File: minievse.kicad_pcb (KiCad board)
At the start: 2 copper layers, 101.6 x 50.8 mm, 54 parts, among them IC1 ATMEGA328P-P, P1 SERIAL, P2 5V input, P3 ICSP, P4 Pilot, P5 AC_GND_AC, P6 LED_STRIP, P7 RELAY_COIL, SW1 RESET_BUTTON, U1 MAX232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

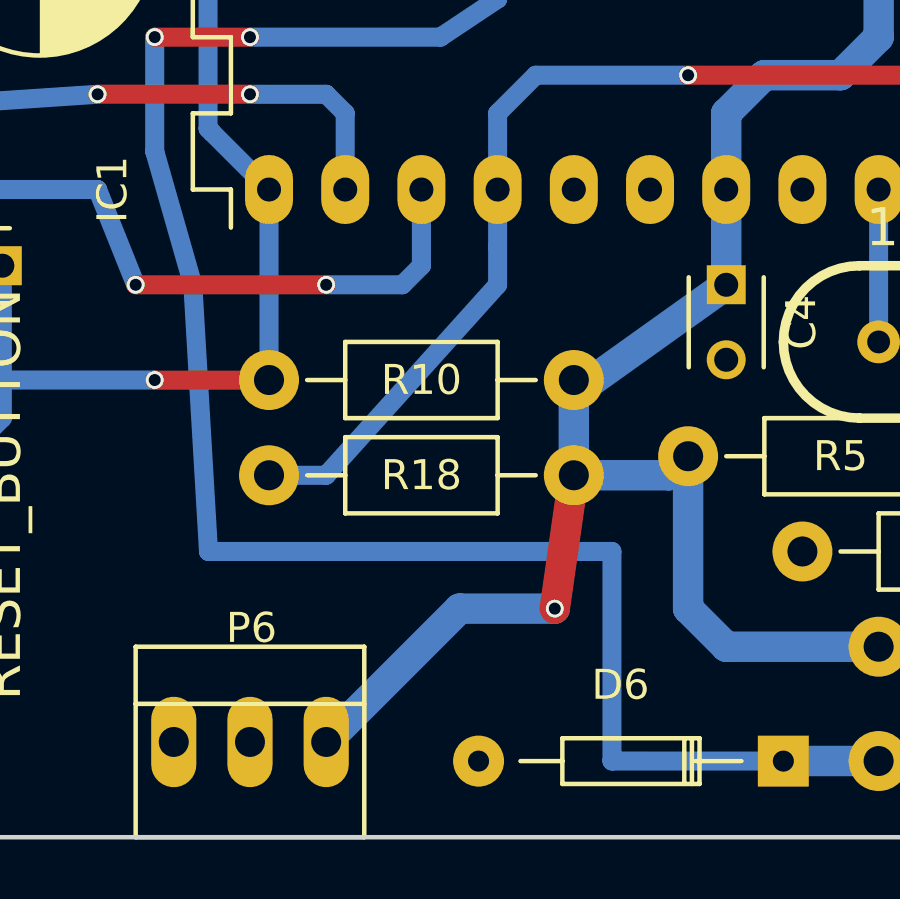
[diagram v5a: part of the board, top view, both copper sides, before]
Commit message: change LED pin from 12 to 6 for wiring convenience
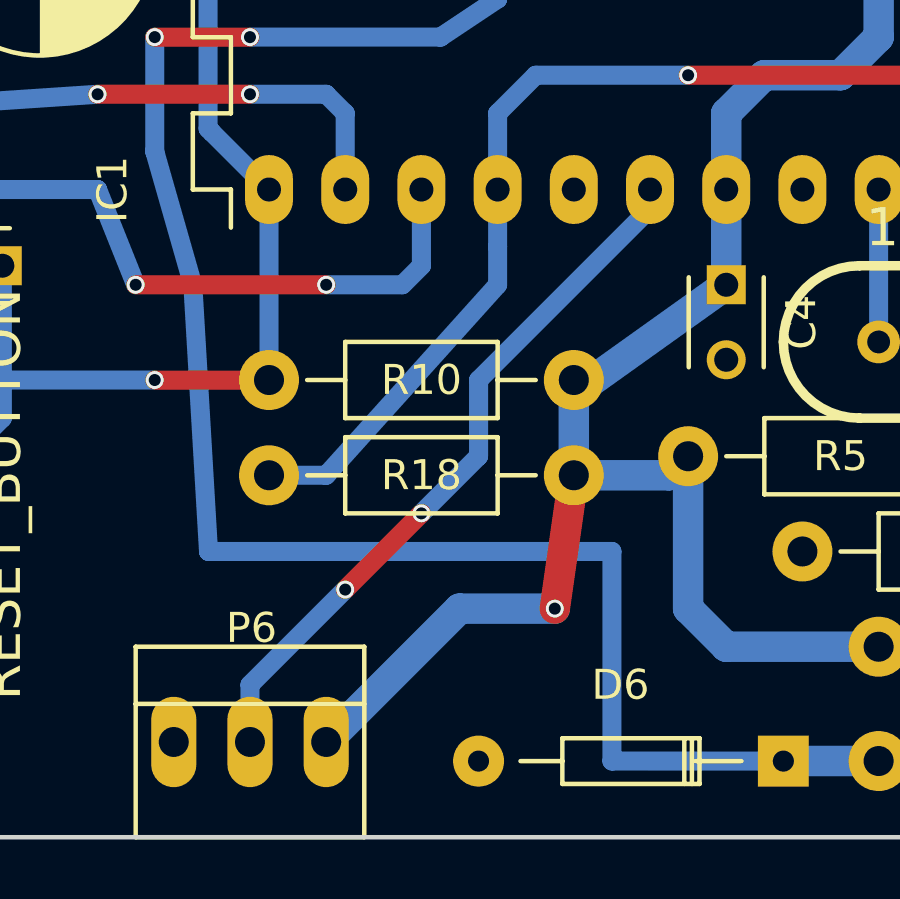
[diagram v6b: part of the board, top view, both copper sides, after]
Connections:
- IC1 pad 12: /LED_DATA -> Net-(IC1-Pad12)
- IC1 pad 6: Net-(IC1-Pad6) -> /LED_DATA
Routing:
- net /LED_DATA: track 0.00 -> 23.9 mm, vias 0 -> 2

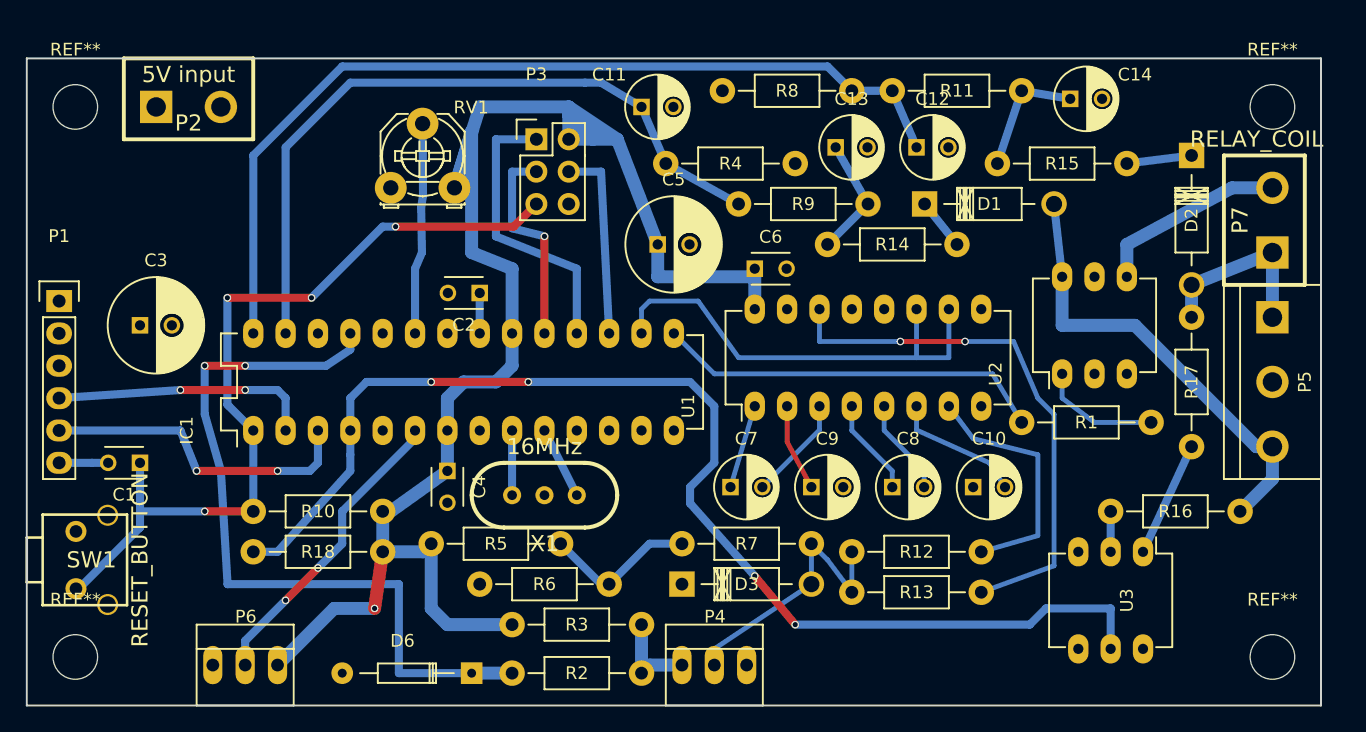
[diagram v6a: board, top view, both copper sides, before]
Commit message: finish wiring up board traces
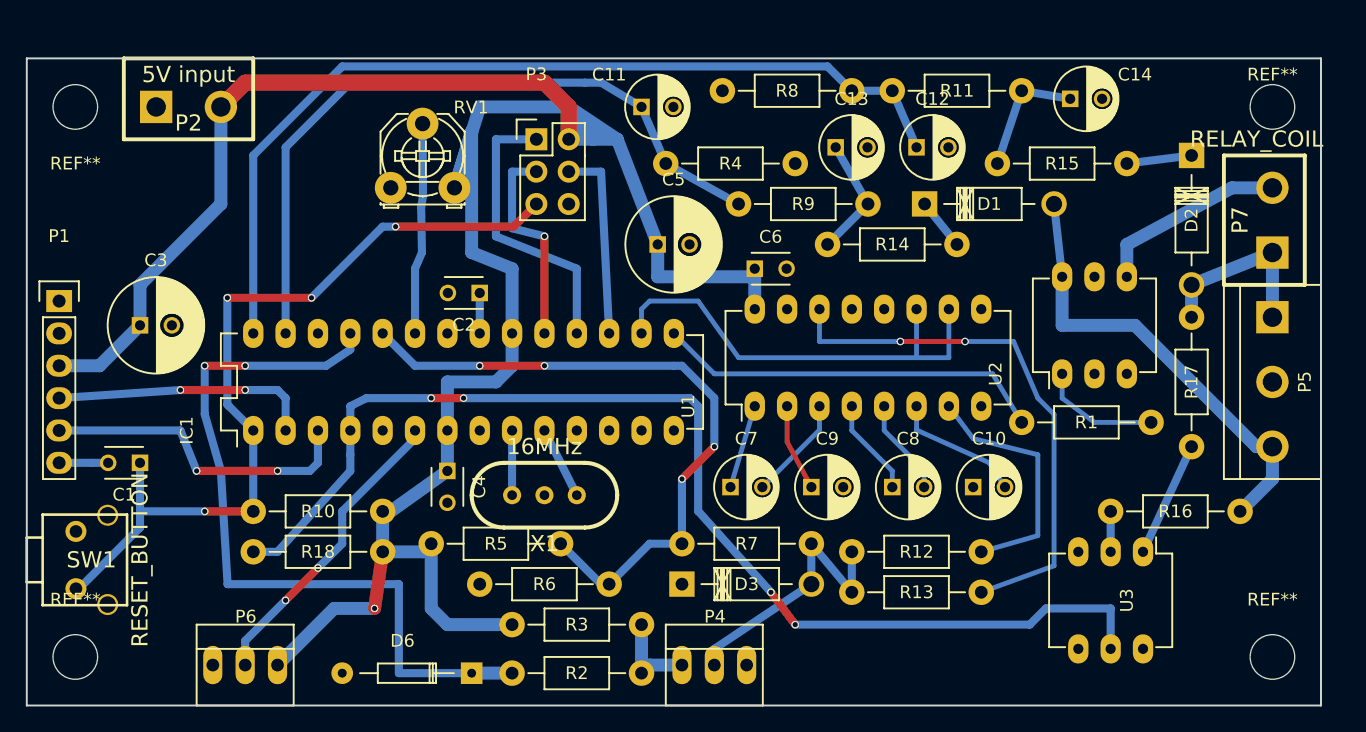
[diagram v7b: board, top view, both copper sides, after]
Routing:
- net +5VD: track 124.5 -> 184.1 mm
- net /PILOTREAD: track 12.2 -> 52.8 mm, vias 0 -> 4
- net /AC_ZEROX: track 95.5 -> 91.7 mm
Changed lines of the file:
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@@
   (general
     (links 105)
-    (no_connects 33)
-    (area 25.324999 25.324999 127.075001 76.275001)
+    (no_connects 29)
+    (area 21.006429 23.005 131.393572 78.445)
     (thickness 1.6)
     (drawings 4)
-    (tracks 244)
+    (tracks 264)
     (zones 0)
     (modules 54)
@@
     (descr "Mounting Hole 3.5mm, no annular")
     (tags "mounting hole 3.5mm no annular")
-    (fp_text reference REF** (at 0 -4.5) (layer F.SilkS)
+    (fp_text reference REF** (at 0 -2.54) (layer F.SilkS)
       (effects (font (size 1 1) (thickness 0.15)))
     )
@@
     (descr "Mounting Hole 3.5mm, no annular")
     (tags "mounting hole 3.5mm no annular")
-    (fp_text reference REF** (at 0 -4.5) (layer F.SilkS)
+    (fp_text reference REF** (at 0 4.445) (layer F.SilkS)
       (effects (font (size 1 1) (thickness 0.15)))
     )
@@
   (segment (start 106.68 46.355) (end 112.395 46.355) (width 1.016) (layer B.Cu) (net 5))
   (segment (start 121.92 55.88) (end 123.19 55.88) (width 1.016) (layer B.Cu) (net 5))
-  (segment (start 86.995 66.67246) (end 86.995 63.5) (width 0.381) (layer B.Cu) (net 6))
-  (segment (start 86.995 63.5) (end 88.265 64.77) (width 0.381) (layer B.Cu) (net 6))
-  (segment (start 88.265 64.77) (end 90.17 67.31) (width 0.381) (layer B.Cu) (net 6) (status 20))
-  (segment (start 90.17 67.31) (end 90.17 64.135) (width 0.381) (layer B.Cu) (net 6) (status 10))
-  (segment (start 79.375 73.025) (end 79.375 71.755) (width 0.254) (layer B.Cu) (net 6))
-  (segment (start 79.375 71.755) (end 86.995 66.67246) (width 0.381) (layer B.Cu) (net 6))
+  (segment (start 86.995 66.67246) (end 86.995 63.5) (width 0.635) (layer B.Cu) (net 6))
+  (segment (start 86.995 63.5) (end 86.995 63.5) (width 0.381) (layer B.Cu) (net 6) (status C00000))
+  (segment (start 86.995 63.5) (end 90.17 67.31) (width 0.635) (layer B.Cu) (net 6) (status C00020))
+  (segment (start 90.17 67.31) (end 90.17 64.135) (width 0.635) (layer B.Cu) (net 6) (status 10))
+  (segment (start 79.375 73.025) (end 79.375 71.755) (width 0.635) (layer B.Cu) (net 6))
+  (segment (start 79.375 71.755) (end 86.995 66.67246) (width 0.635) (layer B.Cu) (net 6))
   (segment (start 50.8 46.99) (end 50.8 48.26) (width 0.635) (layer B.Cu) (net 7))
   (segment (start 54.61 73.66) (end 60.32448 73.66254) (width 0.635) (layer B.Cu) (net 7))
@@
   (segment (start 63.5 38.735) (end 63.5 38.735) (width 0.635) (layer B.Cu) (net 18))
   (segment (start 63.5 34.29) (end 63.5 38.735) (width 0.635) (layer B.Cu) (net 18))
+  (segment (start 76.835 63.5) (end 76.835 58.42) (width 0.635) (layer B.Cu) (net 19) (status 400000))
+  (segment (start 76.835 49.53) (end 79.375 52.07) (width 0.635) (layer B.Cu) (net 19))
+  (segment (start 79.375 52.07) (end 79.375 55.88) (width 0.635) (layer B.Cu) (net 19))
+  (via (at 79.375 55.88) (size 0.6) (drill 0.4) (layers F.Cu B.Cu) (net 19))
+  (segment (start 79.375 55.88) (end 76.835 58.42) (width 0.635) (layer F.Cu) (net 19))
+  (via (at 76.835 58.42) (size 0.6) (drill 0.4) (layers F.Cu B.Cu) (net 19))
+  (segment (start 55.88 49.53) (end 53.34 46.99) (width 0.635) (layer B.Cu) (net 19) (status 800000))
+  (segment (start 66.04 49.53) (end 76.2 49.53) (width 0.635) (layer B.Cu) (net 19))
+  (via (at 66.04 49.53) (size 0.6) (drill 0.4) (layers F.Cu B.Cu) (net 19))
+  (segment (start 60.96 49.53) (end 66.04 49.53) (width 0.635) (layer F.Cu) (net 19))
+  (via (at 60.96 49.53) (size 0.6) (drill 0.4) (layers F.Cu B.Cu) (net 19))
+  (segment (start 55.88 49.53) (end 60.96 49.53) (width 0.635) (layer B.Cu) (net 19))
+  (segment (start 76.2 49.53) (end 76.835 49.53) (width 0.635) (layer B.Cu) (net 19))
   (segment (start 76.835 63.5) (end 74.295 63.5) (width 0.635) (layer B.Cu) (net 19))
   (segment (start 74.295 63.5) (end 71.12 66.675) (width 0.635) (layer B.Cu) (net 19))
@@
   (segment (start 73.66 73.66) (end 74.295 73.025) (width 1.016) (layer B.Cu) (net 22))
   (segment (start 74.295 73.025) (end 76.835 73.025) (width 1.016) (layer B.Cu) (net 22))
+  (segment (start 40.64 29.21) (end 40.64 36.83) (width 1.016) (layer B.Cu) (net 25) (status 400000))
+  (segment (start 34.29 43.18) (end 34.29 46.355) (width 1.016) (layer B.Cu) (net 25) (status 800000))
+  (segment (start 40.64 36.83) (end 34.29 43.18) (width 1.016) (layer B.Cu) (net 25))
+  (segment (start 34.29 46.355) (end 31.115 49.53) (width 1.016) (layer B.Cu) (net 25) (status 400000))
+  (segment (start 31.115 49.53) (end 27.94 49.53) (width 1.016) (layer B.Cu) (net 25) (status 800000))
+  (segment (start 67.945 31.75) (end 67.945 29.21) (width 1.27) (layer F.Cu) (net 25) (status 400000))
+  (segment (start 42.545 27.305) (end 40.64 29.21) (width 1.27) (layer F.Cu) (net 25) (status 800000))
+  (segment (start 66.04 27.305) (end 42.545 27.305) (width 1.27) (layer F.Cu) (net 25))
+  (segment (start 67.945 29.21) (end 66.04 27.305) (width 1.27) (layer F.Cu) (net 25))
   (segment (start 45.085 73.025) (end 49.53 68.58) (width 1.016) (layer B.Cu) (net 25))
   (segment (start 52.705 68.58) (end 53.34 64.135) (width 1.016) (layer F.Cu) (net 25))
@@
   (segment (start 71.755 31.75) (end 67.945 29.21) (width 1.016) (layer B.Cu) (net 25))
   (segment (start 63.5 46.99) (end 63.5 49.53) (width 1.016) (layer B.Cu) (net 25))
-  (segment (start 58.42 52.07) (end 58.42 54.61) (width 1.016) (layer B.Cu) (net 25))
-  (segment (start 59.69 50.8) (end 58.42 52.07) (width 1.016) (layer B.Cu) (net 25))
-  (segment (start 62.23 50.8) (end 59.69 50.8) (width 1.016) (layer B.Cu) (net 25))
+  (segment (start 58.42 50.8) (end 58.42 54.61) (width 1.016) (layer B.Cu) (net 25) (status 800000))
+  (segment (start 58.42 50.8) (end 58.42 50.8) (width 1.016) (layer B.Cu) (net 25))
+  (segment (start 62.23 50.8) (end 58.42 50.8) (width 1.016) (layer B.Cu) (net 25))
   (segment (start 63.5 49.53) (end 62.23 50.8) (width 1.016) (layer B.Cu) (net 25))
   (segment (start 63.5 46.99) (end 63.5 41.91) (width 1.016) (layer B.Cu) (net 25))
@@
   (segment (start 116.84 33.02) (end 111.76 33.655) (width 0.635) (layer B.Cu) (net 37) (status 20))
   (segment (start 50.8 56.515) (end 50.8 57.785) (width 0.635) (layer B.Cu) (net 38))
-  (segment (start 50.8 54.61) (end 50.8 52.07) (width 0.635) (layer B.Cu) (net 38))
+  (segment (start 50.8 54.61) (end 50.8 52.705) (width 0.635) (layer B.Cu) (net 38) (status 400000))
   (segment (start 110.49 68.58) (end 105.41 68.58) (width 0.635) (layer B.Cu) (net 38))
-  (segment (start 82.55 66.04) (end 85.725 69.85) (width 0.635) (layer F.Cu) (net 38))
+  (segment (start 83.82 67.31) (end 85.725 69.85) (width 0.635) (layer F.Cu) (net 38))
   (via (at 85.725 69.85) (size 0.6) (drill 0.4) (layers F.Cu B.Cu) (net 38))
   (segment (start 110.49 68.58) (end 110.49 71.755) (width 0.635) (layer B.Cu) (net 38))
   (segment (start 104.14 69.85) (end 85.725 69.85) (width 0.635) (layer B.Cu) (net 38))
   (segment (start 105.41 68.58) (end 104.14 69.85) (width 0.635) (layer B.Cu) (net 38))
-  (segment (start 82.55 66.04) (end 82.55 66.04) (width 0.635) (layer F.Cu) (net 38))
-  (via (at 82.55 66.04) (size 0.6) (drill 0.4) (layers F.Cu B.Cu) (net 38))
-  (segment (start 77.47 60.325) (end 82.55 66.04) (width 0.635) (layer B.Cu) (net 38))
-  (segment (start 77.47 59.055) (end 77.47 60.325) (width 0.635) (layer B.Cu) (net 38))
-  (segment (start 79.375 57.15) (end 77.47 59.055) (width 0.635) (layer B.Cu) (net 38))
-  (segment (start 79.375 52.705) (end 79.375 57.15) (width 0.635) (layer B.Cu) (net 38))
-  (segment (start 77.47 50.8) (end 79.375 52.705) (width 0.635) (layer B.Cu) (net 38))
-  (segment (start 64.77 50.8) (end 77.47 50.8) (width 0.635) (layer B.Cu) (net 38))
-  (via (at 64.77 50.8) (size 0.6) (drill 0.4) (layers F.Cu B.Cu) (net 38))
-  (segment (start 57.15 50.8) (end 64.77 50.8) (width 0.635) (layer F.Cu) (net 38))
-  (via (at 57.15 50.8) (size 0.6) (drill 0.4) (layers F.Cu B.Cu) (net 38))
-  (segment (start 52.07 50.8) (end 57.15 50.8) (width 0.635) (layer B.Cu) (net 38))
-  (segment (start 50.8 52.07) (end 52.07 50.8) (width 0.635) (layer B.Cu) (net 38))
+  (segment (start 83.82 67.31) (end 83.82 67.31) (width 0.635) (layer F.Cu) (net 38))
+  (via (at 83.82 67.31) (size 0.6) (drill 0.4) (layers F.Cu B.Cu) (net 38))
+  (segment (start 78.11935 60.946883) (end 83.82 67.31) (width 0.635) (layer B.Cu) (net 38))
+  (segment (start 78.105 52.705) (end 78.105 60.96) (width 0.635) (layer B.Cu) (net 38))
+  (segment (start 77.47 52.07) (end 78.105 52.705) (width 0.635) (layer B.Cu) (net 38))
+  (segment (start 59.69 52.07) (end 77.47 52.07) (width 0.635) (layer B.Cu) (net 38))
+  (via (at 59.69 52.07) (size 0.6) (drill 0.4) (layers F.Cu B.Cu) (net 38))
+  (segment (start 57.15 52.07) (end 59.69 52.07) (width 0.635) (layer F.Cu) (net 38))
+  (via (at 57.15 52.07) (size 0.6) (drill 0.4) (layers F.Cu B.Cu) (net 38))
+  (segment (start 52.07 52.07) (end 57.15 52.07) (width 0.635) (layer B.Cu) (net 38))
+  (segment (start 50.8 52.705) (end 52.07 52.07) (width 0.635) (layer B.Cu) (net 38))
   (segment (start 50.8 54.61) (end 50.8 56.515) (width 0.635) (layer B.Cu) (net 38))
   (segment (start 50.8 57.785) (end 45.085 64.135) (width 0.635) (layer B.Cu) (net 38) (status 20))
